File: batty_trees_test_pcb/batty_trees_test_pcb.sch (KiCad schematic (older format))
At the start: 0 parts

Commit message: power and references section 95% done
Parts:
- added X?: PLCC_84, MODULE, symbol OSU_SIM_BASIC:PLCC_84
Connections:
- new net GND: X?.12 (PIN12), X?.13 (PIN13), X?.14 (PIN14), X?.15 (PIN15), X?.19 (PIN19), X?.21 (PIN21), X?.23 (PIN23), X?.25 (PIN25), X?.29 (PIN29), X?.30 (PIN30), X?.31 (PIN31), X?.32 (PIN32), X?.53 (PIN53), X?.54 (PIN54), X?.55 (PIN55), X?.56 (PIN56), X?.57 (PIN57), X?.58 (PIN58), X?.59 (PIN59), X?.64 (PIN64), X?.69 (PIN69), X?.70 (PIN70), X?.71 (PIN71), X?.72 (PIN72), X?.73 (PIN73), X?.74 (PIN74), X?.75 (PIN75), X?.77 (PIN77)
- new net VDD: X?.11 (PIN11)
- new net VDDA: X?.22 (PIN22)
- new net dd_clk: X?.63 (PIN63)
- new net dd_direction: X?.62 (PIN62)
- new net dd_latch_out: X?.60 (PIN60)
- new net dd_lin: X?.51 (PIN51)
- new net dd_pulse_width8: X?.76 (PIN76)
- new net dd_rin: X?.52 (PIN52)
- new net dd_valid: X?.61 (PIN61)
- new net dd_vref: X?.46 (PIN46)
- new net decay_clk: X?.27 (PIN27)
- new net l_fast_clk: X?.81 (PIN81)
- new net l_fast_data_load: X?.80 (PIN80)
- new net l_fast_data_out: X?.79 (PIN79)
- new net l_fast_valid_out: X?.78 (PIN78)
- new net l_slow_clk: X?.10 (PIN10)
- new net l_slow_data_load: X?.9 (PIN9)
- new net l_slow_data_out: X?.8 (PIN8)
- new net l_slow_valid_out: X?.7 (PIN7)
- new net l_vinn: X?.20 (PIN20)
- new net l_vinp: X?.18 (PIN18)
- new net l_vpulse1: X?.6 (PIN6)
- new net l_vpulse2: X?.5 (PIN5)
- new net l_vpulse3: X?.4 (PIN4)
- new net l_vpulse4: X?.3 (PIN3)
- new net l_vpulse5: X?.68 (PIN68)
- new net l_vpulse6: X?.67 (PIN67)
- new net l_vpulse7: X?.66 (PIN66)
- new net l_vpulse8: X?.65 (PIN65)
- new net mux_sel: X?.2 (PIN2)
- new net r_vinn: X?.24 (PIN24)
- new net r_vinp: X?.26 (PIN26)
- new net r_vpulse1: X?.38 (PIN38)
- new net r_vpulse2: X?.39 (PIN39)
- new net r_vpulse3: X?.40 (PIN40)
- new net r_vpulse4: X?.41 (PIN41)
- new net r_vpulse5: X?.42 (PIN42)
- new net r_vpulse6: X?.43 (PIN43)
- new net r_vpulse7: X?.44 (PIN44)
- new net r_vpulse8: X?.45 (PIN45)
- new net rate_crtl: X?.28 (PIN28)
- new net right_fast_clk: X?.47 (PIN47)
- new net right_fast_data_load: X?.48 (PIN48)
- new net right_fast_data_out: X?.49 (PIN49)
- new net right_fast_valid_out: X?.50 (PIN50)
- new net right_slow_clk: X?.34 (PIN34)
- new net right_slow_data_load: X?.35 (PIN35)
- new net right_slow_data_out: X?.36 (PIN36)
- new net right_slow_valid_out: X?.37 (PIN37)
- new net rst: X?.16 (PIN16)
- new net ser_test: X?.33 (PIN33)
- new net sipo_clk: X?.84 (PIN84)
- new net sipo_clkb: X?.1 (PIN1)
- new net sipo_sin: X?.83 (PIN83)
- new net sipo_sout: X?.82 (PIN82)
- new net vgr: X?.17 (PIN17)

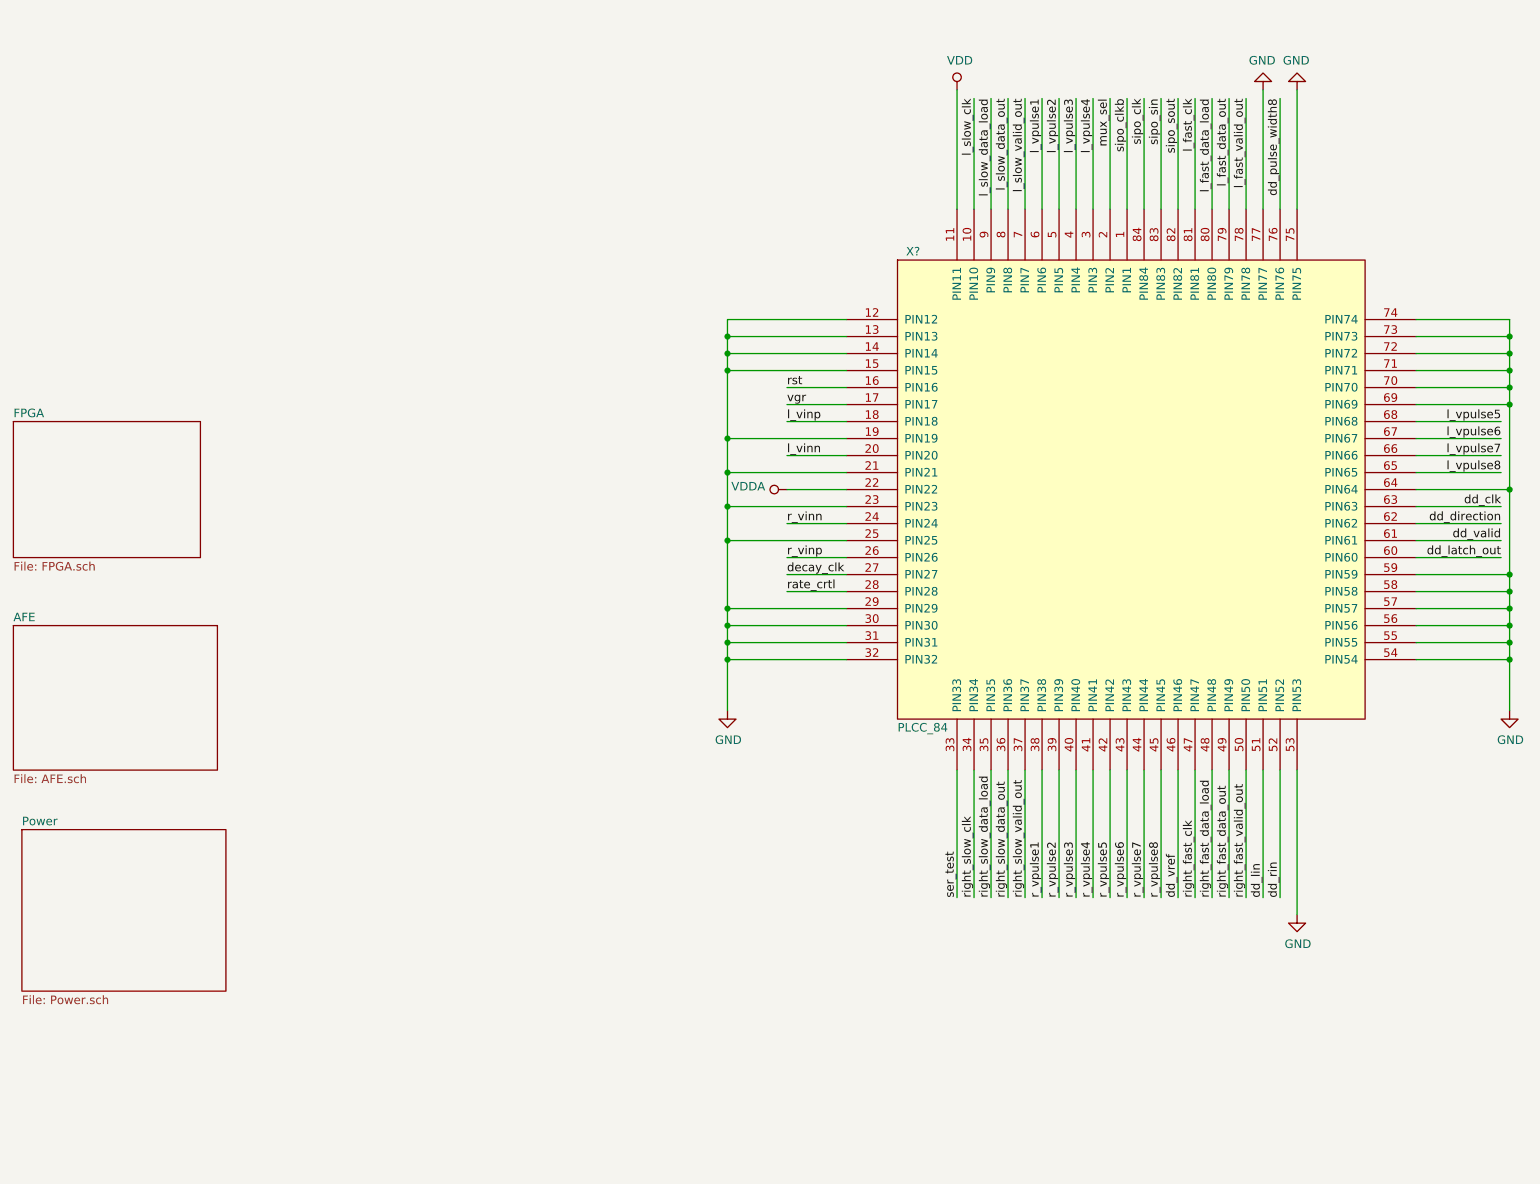
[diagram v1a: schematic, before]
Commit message: Finished off Power section and made up AFE schematic
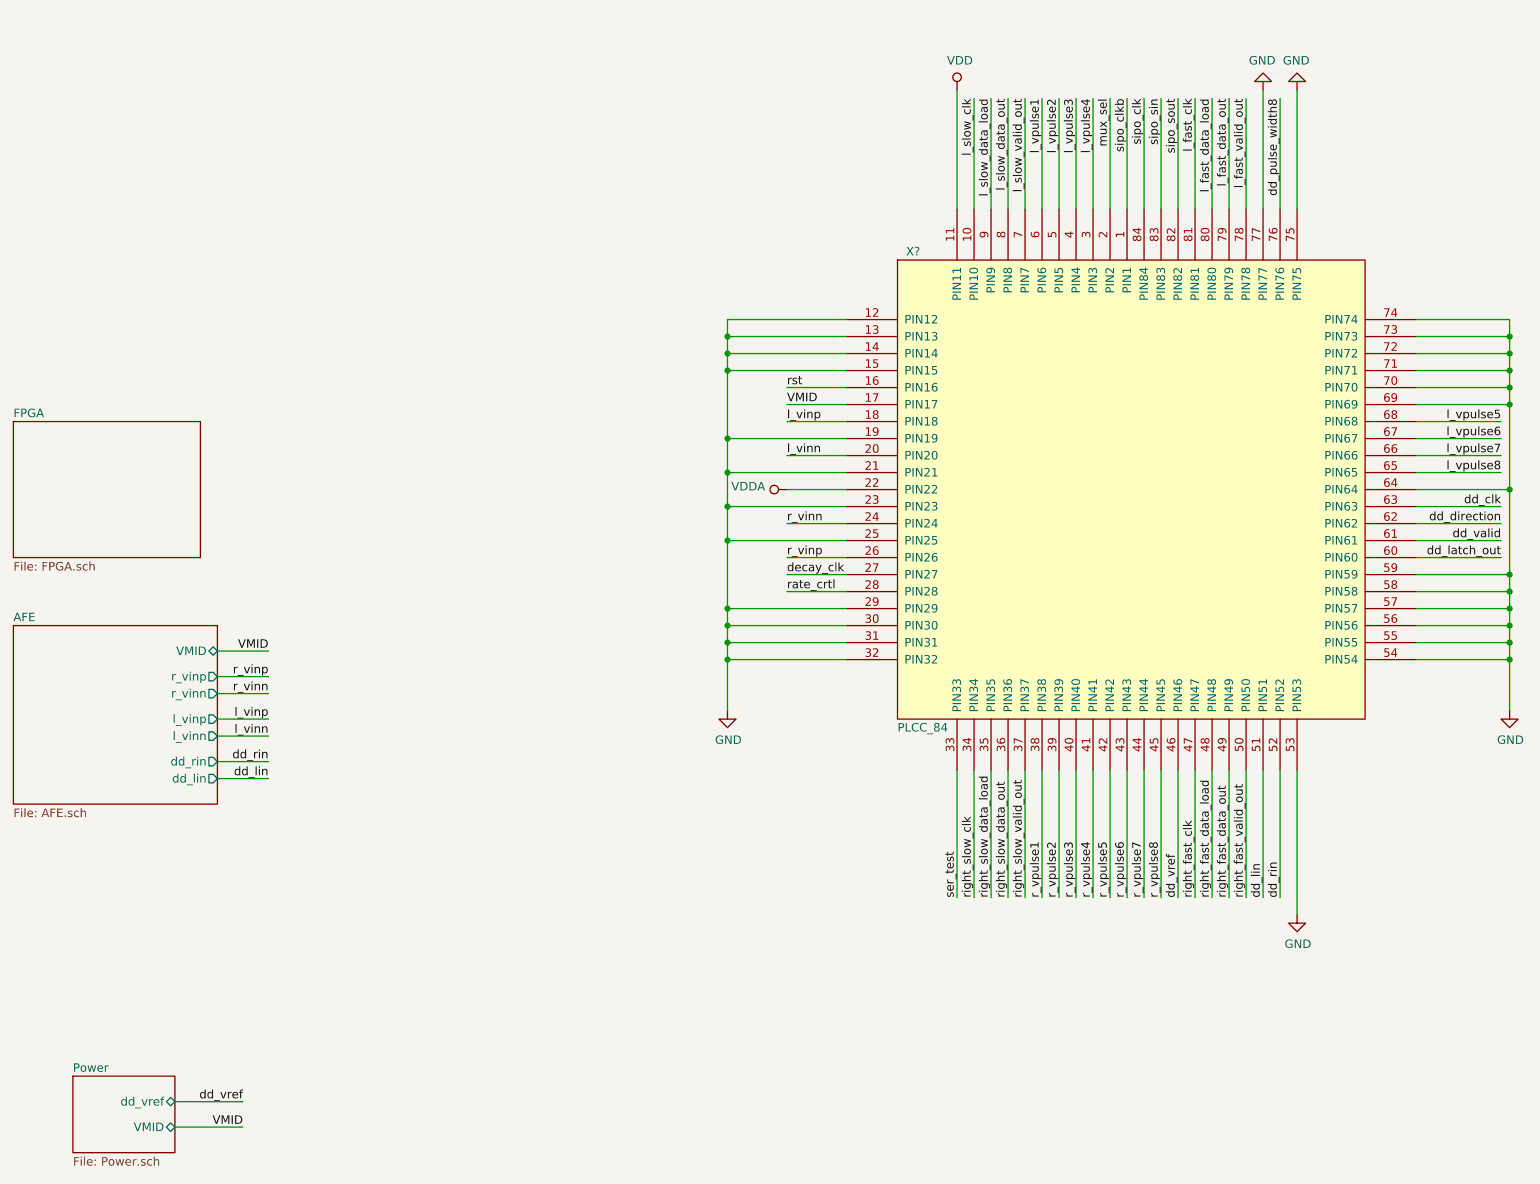
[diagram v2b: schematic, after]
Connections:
- net vgr renamed VMID
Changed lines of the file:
@@
 $EndDescr
 $Sheet
-S 1500 4400 1200 850
+S 1500 4400 1200 1050
 U 5F370A72
 F0 "AFE" 50
 F1 "AFE.sch" 50
+F2 "VMID" B R 2700 4550 50
+F3 "r_vinp" O R 2700 4700 50
+F4 "r_vinn" O R 2700 4800 50
+F5 "l_vinp" O R 2700 4950 50
+F6 "l_vinn" O R 2700 5050 50
+F7 "dd_rin" O R 2700 5200 50
+F8 "dd_lin" O R 2700 5300 50
 $EndSheet
 $Comp
@@
 Text Label 7550 1300 3    50   ~ 0
 l_vpulse1
-$Sheet
-S 1550 5600 1200 950
-U 5F3A707E
-F0 "Power" 50
-F1 "Power.sch" 50
-$EndSheet
 Text Label 7750 1300 3    50   ~ 0
 l_vpulse3
@@
 Text Label 6050 3200 0    50   ~ 0
 l_vinp
-Text Label 6050 3100 0    50   ~ 0
-vgr
 Text Label 6050 3000 0    50   ~ 0
 rst
@@
 Wire Wire Line
 	9750 2700 10300 2700
+Wire Wire Line
+	2450 7350 2850 7350
+Wire Wire Line
+	2450 7200 2850 7200
+$Sheet
+S 1850 7050 600  450
+U 5F3A707E
+F0 "Power" 50
+F1 "Power.sch" 50
+F2 "dd_vref" B R 2450 7200 50
+F3 "VMID" B R 2450 7350 50
+$EndSheet
+Text Label 2850 7200 2    50   ~ 0
+dd_vref
+Text Label 2850 7350 2    50   ~ 0
+VMID
+Text Label 6050 3100 0    50   ~ 0
+VMID
+Wire Wire Line
+	2700 5200 3000 5200
+Wire Wire Line
+	2700 5300 3000 5300
+Text Label 3000 5200 2    50   ~ 0
+dd_rin
+Text Label 3000 5300 2    50   ~ 0
+dd_lin
+Wire Wire Line
+	2700 5050 3000 5050
+Wire Wire Line
+	2700 4950 3000 4950
+Wire Wire Line
+	2700 4800 3000 4800
+Wire Wire Line
+	2700 4700 3000 4700
+Wire Wire Line
+	2700 4550 3000 4550
+Text Label 3000 4550 2    50   ~ 0
+VMID
+Text Label 3000 4700 2    50   ~ 0
+r_vinp
+Text Label 3000 4800 2    50   ~ 0
+r_vinn
+Text Label 3000 4950 2    50   ~ 0
+l_vinp
+Text Label 3000 5050 2    50   ~ 0
+l_vinn
 $EndSCHEMATC

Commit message: wired up chip to fpga on schematic and begininng to do layout
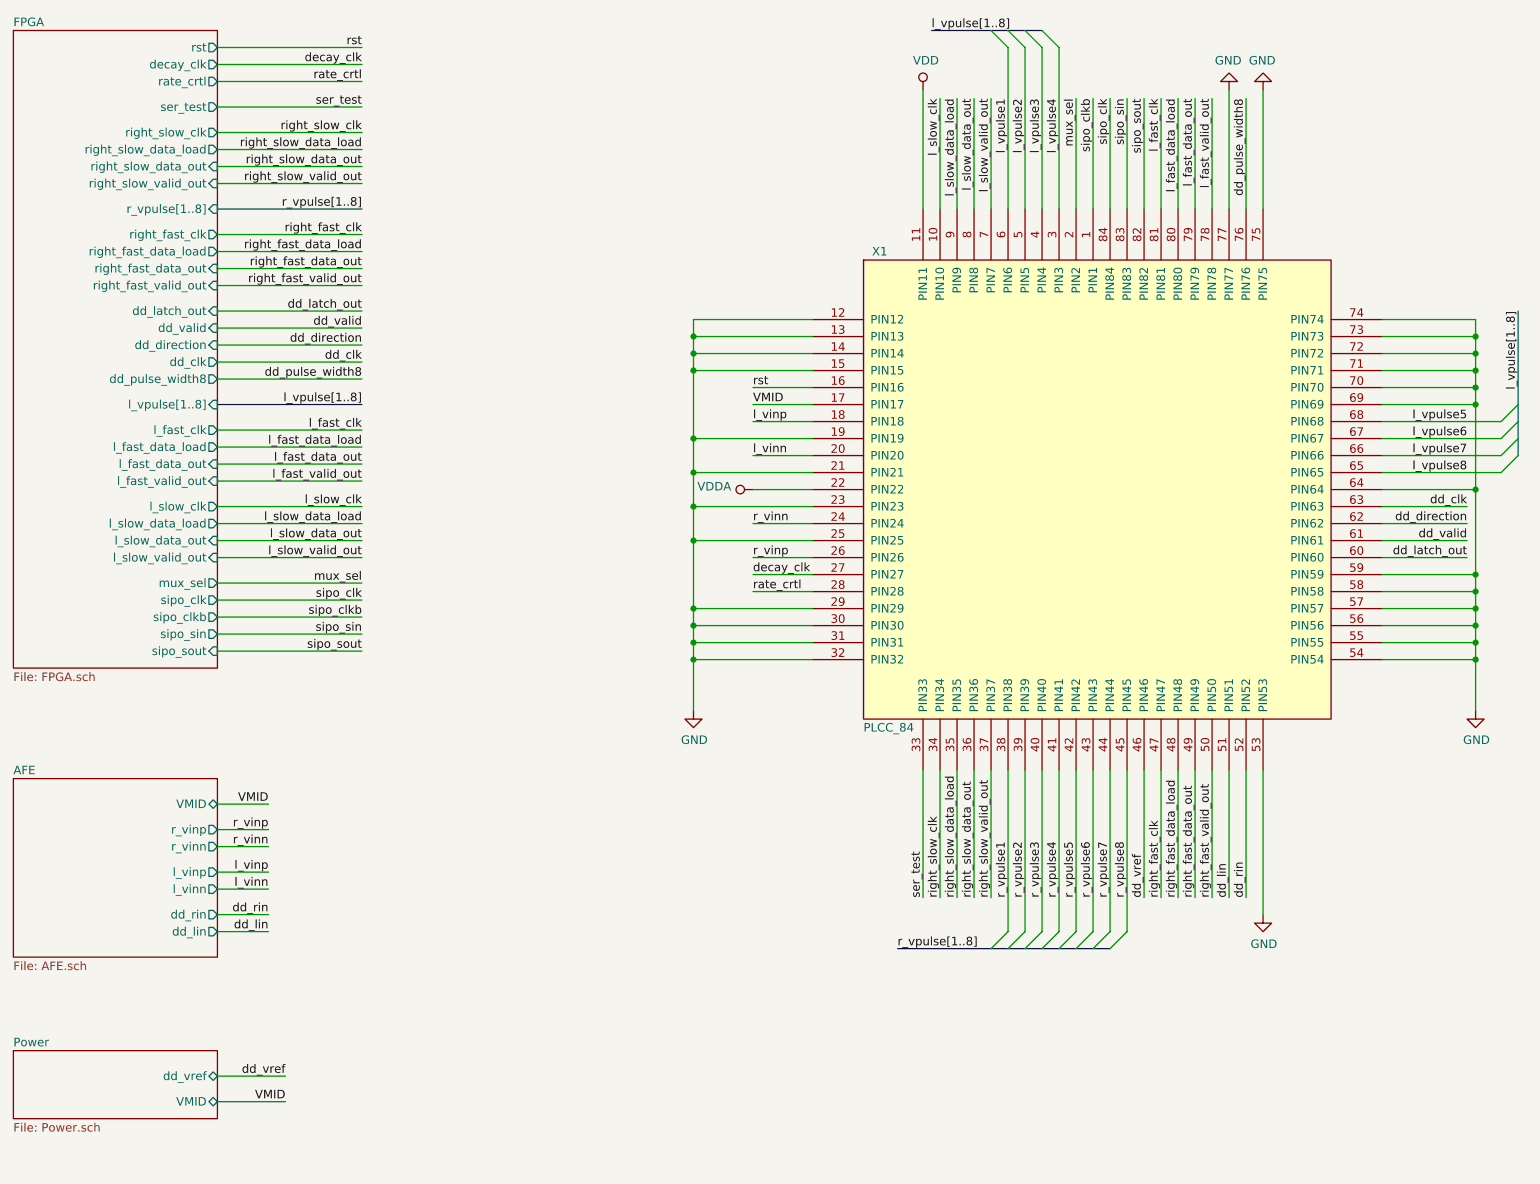
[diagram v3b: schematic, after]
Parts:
- X1: renamed from X?; footprint MODULE -> OSU_SIM_BASIC:PLCC_84POS
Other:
- moved on the sheet: X1
